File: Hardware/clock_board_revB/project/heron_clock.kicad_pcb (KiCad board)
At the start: 4 copper layers, 118 x 44 mm, 110 parts, among them J1 5V_IN, J10 PPS_B200_2, J2 PPS_IN, J3 REF_B210_1, J4 REF_B210_2, J5 REF_B200_1, J6 REF_B200_2, J7 PPS_B210_1, J8 PPS_B210_2, J9 PPS_B200_1, U1 TPS7A2033DBVR, U2 TPS7A2033DBVR, U3 SiT5155AI-FK-33E0-10.000000, U4 LMK1C1104PWR, U5 SN74LVC1G17DBVR, U6 SN74LVC125APWR

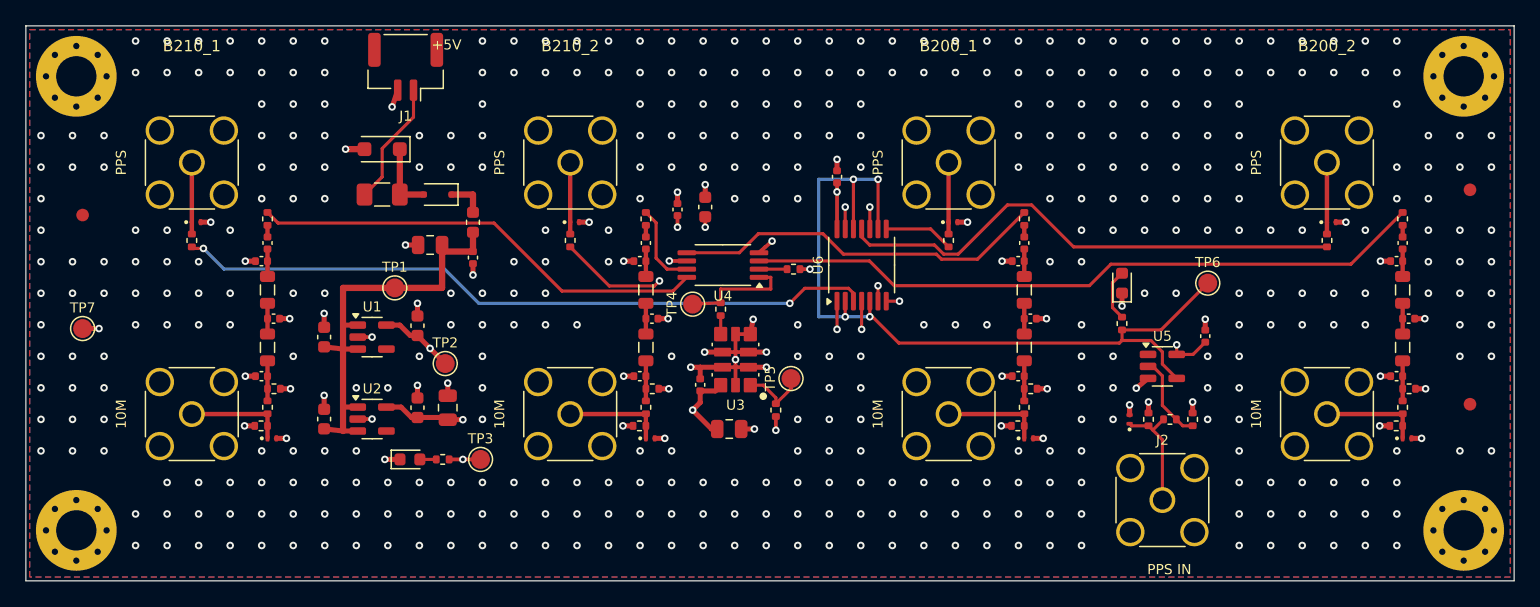
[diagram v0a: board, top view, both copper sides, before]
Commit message: Change clock board rev B SDR jacks to SMP blind-mate (D-027)
Change J3-J10 from vertical SMA jacks to Amphenol RF SMP-MSLD-PCT
limited-detent jacks. J2 (PPS IN) stays SMA. The new footprint has
oversize holes (+/-0.20 mm float), so each jack is soldered in place
with its SDR mated. Lead sizes come from the Amphenol IGES model.

Swap the footprints in the existing PCB and keep all routes. Refill
the pours. Move the board title 0.5 mm clear of the larger pads.
Set the R23 DNP flag to match the schematic. Save in KiCad 10 format.
DRC: 0 errors, 0 unconnected pads, 0 parity issues.

Add an export-only mode to make_fab.sh, and let it run on Windows.
Record D-027 and the open values (Q-015) in docs/DECISIONS.md.

Co-Authored-By: Claude Opus 5.5 <noreply@anthropic.com>
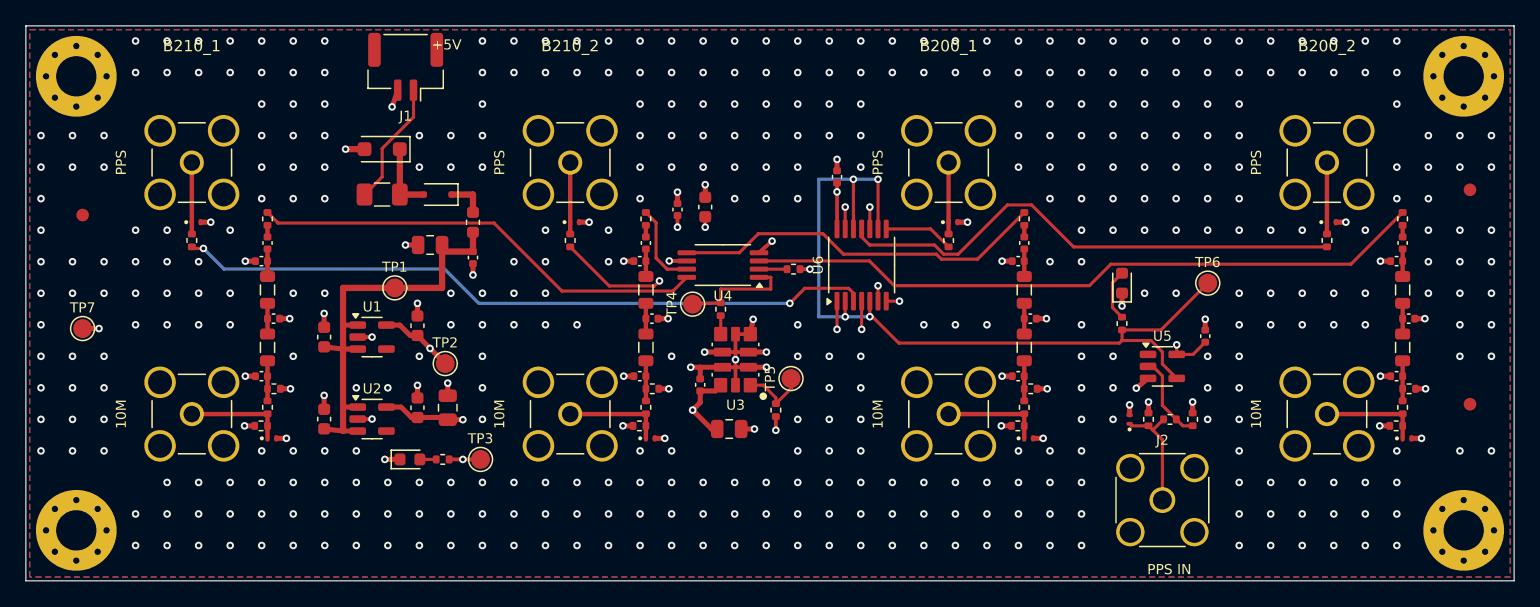
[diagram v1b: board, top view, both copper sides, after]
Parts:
- J10, J3, J4, J5, J6, J7, J8, J9: footprint Connector_Coaxial:SMA_Amphenol_132134_Vertical -> HERON_Clock:SMP_Amphenol_SMP-MSLD-PCT_Vertical_Float

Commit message: Update clock board rev B BOM, jacks and LDOs for direct SMP mate (D-027)
Change J3-J10 to Amphenol SMP-MSSB-PCT (smooth bore). Take the
footprint dimensions from the Amphenol outline drawing rev B.
Each SDR now uses one Cinch 134-1019-451 SMA-to-SMP adapter. There
is no bullet.

Bring the BOM up to date. Give every resistor an MPN and a tolerance.
Replace parts that are obsolete or have no stock: the 1 uF, 2.2 uF,
10 uF and 100 nF capacitors and D2. Replace U1 with LP5907MFX-3.3 and
U2 with TLV75533PDBVR, because TPS7A2033PDBVR has no stock (same
pinout). Add bom_sources.csv for stock, price, notes and the
off-board adapters. make_bom.py fails when a fitted part has no MPN.

Regenerate the schematic from design.py and sync the PCB fields.
Restore the SMP assembly note. DRC: 0 errors, 0 parity issues.

Co-Authored-By: Claude Opus 5.5 <noreply@anthropic.com>
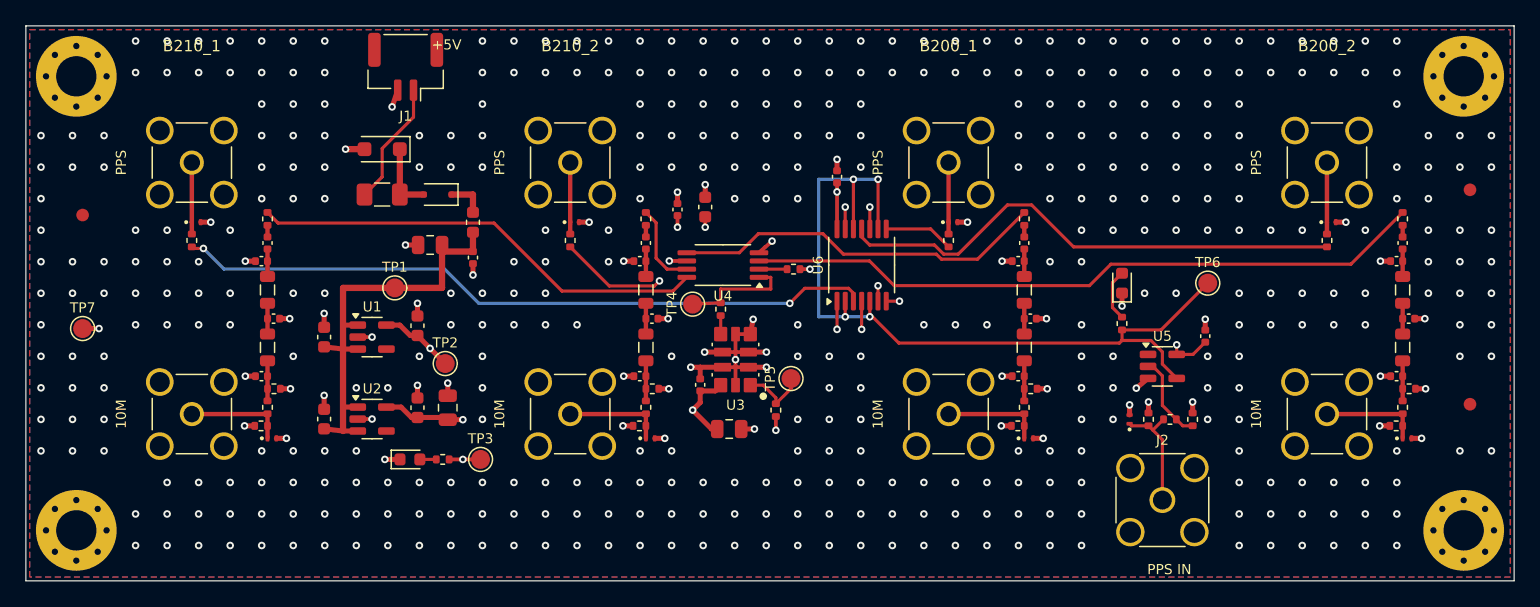
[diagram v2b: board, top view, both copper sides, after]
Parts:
- D2: value PMEG3020EJ -> SS1030HEWS
- J10, J3, J4, J5, J6, J7, J8, J9: footprint HERON_Clock:SMP_Amphenol_SMP-MSLD-PCT_Vertical_Float -> HERON_Clock:SMP_Amphenol_SMP-MSSB-PCT_Vertical_Float
- U1: value TPS7A2033DBVR -> LP5907MFX-3.3/NOPB
- U2: value TPS7A2033DBVR -> TLV75533PDBVR

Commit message: Change clock board SMP jacks to SMP-MSSB-PCT10T and L1-L8 to Abracon
J3-J10 change from Amphenol SMP-MSSB-PCT ($29) to SMP-MSSB-PCT10T
($6.89). The legs stay through-hole in +/-0.2 mm float holes. The
signal contact is now a surface-mount tab, so the footprint gets a
tab pad (no paste) and the copper keep-out from the Amphenol drawing.
All jacks have the tab toward +x. The 10 MHz traces end on the tab.
The PPS jacks get a dog-leg to the ESD diode; J9 goes through two
vias on B.Cu because PPS4_Y passes next to it.

L1-L8 change from Coilcraft 0805CS-821XJRC (Digi-Key Marketplace
only) to Abracon AISC-0805-R82J-T (same size, core and specs).

DRC: 0 errors, 0 unconnected pads, 0 parity issues. Courtyard
overlaps at the 10 MHz jack tab side and starved thermals on some
leg pads remain as warnings (see the README).

Co-Authored-By: Claude Opus 5.5 <noreply@anthropic.com>
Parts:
- J10, J3, J4, J5, J6, J7, J8, J9: footprint HERON_Clock:SMP_Amphenol_SMP-MSSB-PCT_Vertical_Float -> HERON_Clock:SMP_Amphenol_SMP-MSSB-PCT10T_Vertical_Float
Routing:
- net Net-(D12-A1): track 5.66 -> 16.7 mm, vias 0 -> 2
- net Net-(D13-A1): track 5.66 -> 10.9 mm
- net Net-(D11-A1): track 5.66 -> 10.9 mm
- net Net-(D10-A1): track 5.67 -> 10.9 mm
- net Net-(D7-A1): track 7.98 -> 4.46 mm
- net Net-(D6-A1): track 8.01 -> 4.50 mm
- net Net-(D5-A1): track 7.98 -> 4.46 mm
- net Net-(D4-A1): track 7.98 -> 4.46 mm
